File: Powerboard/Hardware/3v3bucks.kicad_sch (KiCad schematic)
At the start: 24 parts, among them IC2 SiC437BED-T1-GE3, Q5 PXP012-30QLJ, Q6 PXP012-30QLJ, U1 LTC4412xS6, U8 LTC4412xS6

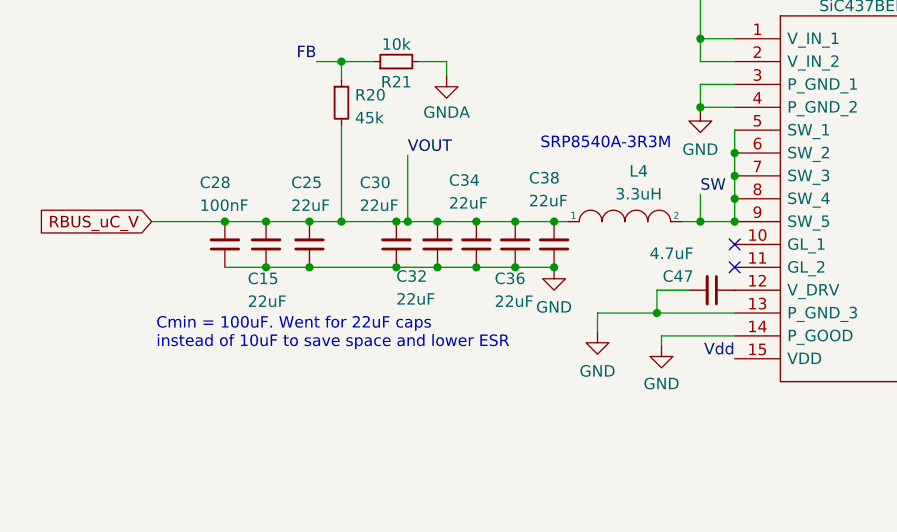
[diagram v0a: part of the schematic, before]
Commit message: removed 100nf cap, pgood pull up
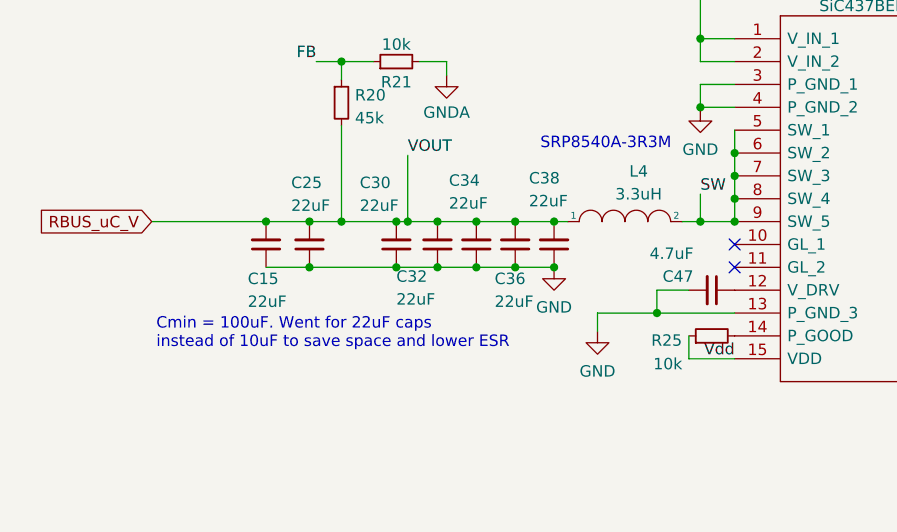
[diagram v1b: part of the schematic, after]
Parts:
- removed C28: 100nF, Capacitor_SMD:C_0402_1005Metric, symbol Device:C_Small
- added R25: 10k, Resistor_SMD:R_0402_1005Metric, symbol Device:R_Small
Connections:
- net GND: no longer IC2.14 (P_GOOD)
- net Vdd: now also R25.1
- new net: IC2.14 (P_GOOD), R25.2
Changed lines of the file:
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@@
   (junction (at 260.858 50.038) (diameter 0) (color 0 0 0 0)
   )
-  (junction (at 63.246 117.348) (diameter 0) (color 0 0 0 0)
-  )
   (junction (at 111.506 112.268) (diameter 0) (color 0 0 0 0)
   )
   (junction (at 63.246 112.268) (diameter 0) (color 0 0 0 0)
-  )
-  (junction (at 58.674 112.268) (diameter 0) (color 0 0 0 0)
   )
   (junction (at 95.25 117.348) (diameter 0) (color 0 0 0 0)
@@
     (stroke (width 0) (type default))
   )
-  (wire (pts (xy 50.546 112.268) (xy 58.674 112.268))
+  (wire (pts (xy 50.546 112.268) (xy 63.246 112.268))
     (stroke (width 0) (type default))
   )
@@
     (stroke (width 0) (type default))
   )
-  (wire (pts (xy 107.188 125.984) (xy 107.188 124.968))
-    (stroke (width 0) (type default))
-  )
   (wire (pts (xy 235.966 77.978) (xy 246.126 77.978))
     (stroke (width 0) (type default))
@@
     (stroke (width 0) (type default))
   )
-  (wire (pts (xy 107.188 124.968) (xy 115.316 124.968))
+  (wire (pts (xy 110.236 127.508) (xy 115.316 127.508))
     (stroke (width 0) (type default))
   )
@@
     (stroke (width 0) (type default))
   )
-  (wire (pts (xy 58.674 112.268) (xy 63.246 112.268))
-    (stroke (width 0) (type default))
-  )
   (wire (pts (xy 86.614 117.348) (xy 90.932 117.348))
     (stroke (width 0) (type default))
   )
-  (wire (pts (xy 58.674 117.348) (xy 63.246 117.348))
-    (stroke (width 0) (type default))
-  )
   (wire (pts (xy 237.236 96.012) (xy 237.236 98.552))
     (stroke (width 0) (type default))
   )
   (wire (pts (xy 276.098 93.472) (xy 262.636 93.472))
+    (stroke (width 0) (type default))
+  )
+  (wire (pts (xy 110.236 124.968) (xy 110.236 127.508))
     (stroke (width 0) (type default))
   )
@@
     )
   )
-  (symbol (lib_id "power:GND") (at 107.188 125.984 0) (unit 1)
-    (in_bom yes) (on_board yes) (dnp no)
-    (property "Reference" "#PWR0105" (at 107.188 132.334 0)
-      (effects (font (size 1.27 1.27)) hide)
-    )
-    (property "Value" "GND" (at 107.188 130.302 0)
-      (effects (font (size 1.27 1.27)))
-    )
-    (property "Footprint" "" (at 107.188 125.984 0)
-      (effects (font (size 1.27 1.27)) hide)
-    )
-    (property "Datasheet" "" (at 107.188 125.984 0)
-      (effects (font (size 1.27 1.27)) hide)
-    )
-    (pin "1")
-    (instances
-      (project "Switcher"
-        (path "/e63e39d7-6ac0-4ffd-8aa3-1841a4541b55/e469982c-3823-4665-9e6d-e90b00c2da09"
-          (reference "#PWR0105") (unit 1)
-        )
-      )
-    )
-  )
   (symbol (lib_id "Power_Management:LTC4412xS6") (at 246.126 67.818 0) (unit 1)
     (in_bom yes) (on_board yes) (dnp no)
@@
     )
   )
-  (symbol (lib_id "Device:C_Small") (at 58.674 114.808 180) (unit 1)
+  (symbol (lib_id "Device:R_Small") (at 112.776 124.968 90) (unit 1)
     (in_bom yes) (on_board yes) (dnp no)
-    (property "Reference" "C28" (at 55.88 107.95 0)
-      (effects (font (size 1.27 1.27)) (justify right))
-    )
-    (property "Value" "100nF" (at 55.88 110.4869 0)
-      (effects (font (size 1.27 1.27)) (justify right))
-    )
-    (property "Footprint" "Capacitor_SMD:C_0402_1005Metric" (at 58.674 114.808 0)
-      (effects (font (size 1.27 1.27)) hide)
-    )
-    (property "Datasheet" "~" (at 58.674 114.808 0)
-      (effects (font (size 1.27 1.27)) hide)
-    )
-    (pin "1")
-    (pin "2")
-    (instances
-      (project "Switcher"
-        (path "/e63e39d7-6ac0-4ffd-8aa3-1841a4541b55/e469982c-3823-4665-9e6d-e90b00c2da09"
-          (reference "C28") (unit 1)
-        )
-      )
+    (property "Reference" "R25" (at 109.474 125.476 90)
+      (effects (font (size 1.27 1.27)) (justify left))
+    )
+    (property "Value" "10k" (at 109.4994 128.0887 90)
+      (effects (font (size 1.27 1.27)) (justify left))
+    )
+    (property "Footprint" "Resistor_SMD:R_0402_1005Metric" (at 112.776 124.968 0)
+      (effects (font (size 1.27 1.27)) hide)
+    )
+    (property "Datasheet" "~" (at 112.776 124.968 0)
+      (effects (font (size 1.27 1.27)) hide)
+    )
+    (pin "1")
+    (pin "2")
+    (instances
+      (project "Switcher"
+        (path "/e63e39d7-6ac0-4ffd-8aa3-1841a4541b55/e469982c-3823-4665-9e6d-e90b00c2da09"
+          (reference "R25") (unit 1)
+        )
+      )

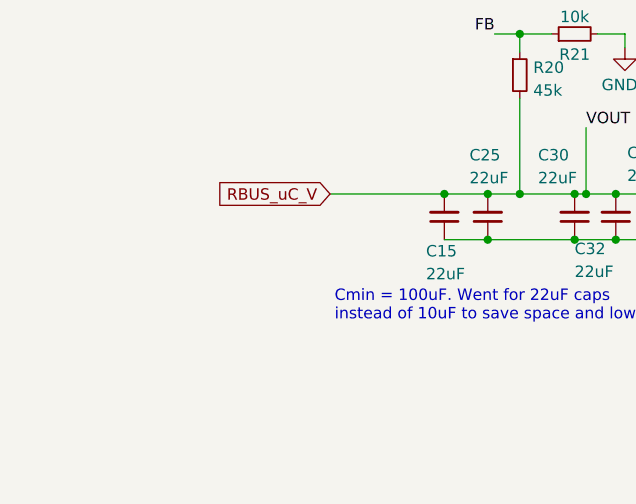
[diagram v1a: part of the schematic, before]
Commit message: 3v3logging moved to buck output
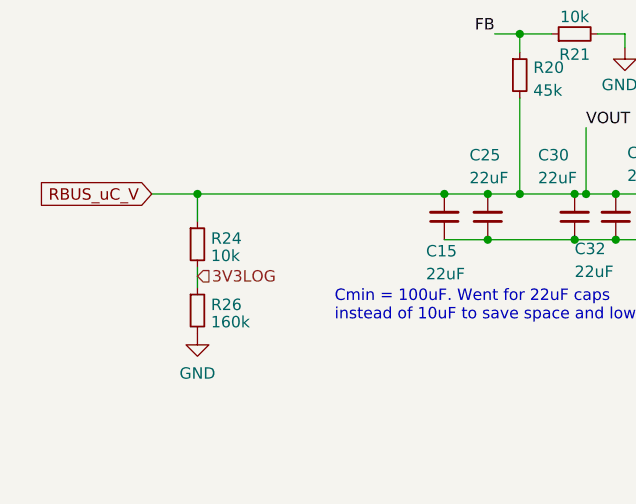
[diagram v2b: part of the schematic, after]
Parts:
- added R24: 10k, Resistor_SMD:R_0402_1005Metric, symbol Device:R_Small
- added R26: 160k, Resistor_SMD:R_0402_1005Metric, symbol Device:R_Small
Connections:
- net GND: now also R26.2
- net RBUS_uC_V: now also R24.1
- new net 3V3LOG: R24.2, R26.1
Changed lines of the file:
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@@
   (junction (at 180.086 107.95) (diameter 0) (color 0 0 0 0)
+  )
+  (junction (at 35.814 112.268) (diameter 0) (color 0 0 0 0)
   )
   (junction (at 260.858 50.038) (diameter 0) (color 0 0 0 0)
@@
     (stroke (width 0) (type default))
   )
-  (wire (pts (xy 50.546 112.268) (xy 63.246 112.268))
+  (wire (pts (xy 30.734 112.268) (xy 35.814 112.268))
     (stroke (width 0) (type default))
   )
@@
     (stroke (width 0) (type default))
   )
+  (wire (pts (xy 35.814 112.268) (xy 63.246 112.268))
+    (stroke (width 0) (type default))
+  )
   (wire (pts (xy 237.236 93.472) (xy 237.236 96.012))
     (stroke (width 0) (type default))
@@
     (stroke (width 0) (type default))
   )
+  (wire (pts (xy 35.814 120.396) (xy 35.814 122.682))
+    (stroke (width 0) (type default))
+  )
   (wire (pts (xy 111.506 83.312) (xy 164.084 83.312))
     (stroke (width 0) (type default))
@@
   )
   (wire (pts (xy 237.744 129.032) (xy 247.904 129.032))
+    (stroke (width 0) (type default))
+  )
+  (wire (pts (xy 35.814 112.268) (xy 35.814 115.316))
     (stroke (width 0) (type default))
   )
@@
     (effects (font (size 1.27 1.27)) (justify right bottom))
   )
-  (global_label "RBUS_uC_V" (shape input) (at 50.546 112.268 180) (fields_autoplaced)
+  (global_label "RBUS_uC_V" (shape input) (at 30.734 112.268 180) (fields_autoplaced)
     (effects (font (size 1.27 1.27)) (justify right))
-    (property "Intersheetrefs" "${INTERSHEET_REFS}" (at 37.6989 112.1886 0)
+    (property "Intersheetrefs" "${INTERSHEET_REFS}" (at 17.8869 112.1886 0)
       (effects (font (size 1.27 1.27)) (justify right) hide)
     )
   )
   (hierarchical_label "USBPOWER" (shape input) (at 258.064 121.412 0) (fields_autoplaced)
+    (effects (font (size 1.27 1.27)) (justify left))
+  )
+  (hierarchical_label "3V3LOG" (shape input) (at 35.814 121.412 0) (fields_autoplaced)
     (effects (font (size 1.27 1.27)) (justify left))
   )
@@
         (path "/e63e39d7-6ac0-4ffd-8aa3-1841a4541b55/e469982c-3823-4665-9e6d-e90b00c2da09"
           (reference "C40") (unit 1)
+        )
+      )
+    )
+  )
+  (symbol (lib_id "power:GND") (at 35.814 127.762 0) (unit 1)
+    (in_bom yes) (on_board yes) (dnp no) (fields_autoplaced)
+    (property "Reference" "#PWR01" (at 35.814 134.112 0)
+      (effects (font (size 1.27 1.27)) hide)
+    )
+    (property "Value" "GND" (at 35.814 132.2054 0)
+      (effects (font (size 1.27 1.27)))
+    )
+    (property "Footprint" "" (at 35.814 127.762 0)
+      (effects (font (size 1.27 1.27)) hide)
+    )
+    (property "Datasheet" "" (at 35.814 127.762 0)
+      (effects (font (size 1.27 1.27)) hide)
+    )
+    (pin "1")
+    (instances
+      (project "Switcher"
+        (path "/e63e39d7-6ac0-4ffd-8aa3-1841a4541b55/133f56f4-a29c-4cbf-87b7-9d99a292e3c0"
+          (reference "#PWR01") (unit 1)
+        )
+        (path "/e63e39d7-6ac0-4ffd-8aa3-1841a4541b55/e469982c-3823-4665-9e6d-e90b00c2da09"
+          (reference "#PWR01") (unit 1)
         )
       )
@@
     )
   )
+  (symbol (lib_id "Device:R_Small") (at 35.814 125.222 0) (unit 1)
+    (in_bom yes) (on_board yes) (dnp no) (fields_autoplaced)
+    (property "Reference" "R26" (at 37.3126 124.5783 0)
+      (effects (font (size 1.27 1.27)) (justify left))
+    )
+    (property "Value" "160k" (at 37.3126 126.4993 0)
+      (effects (font (size 1.27 1.27)) (justify left))
+    )
+    (property "Footprint" "Resistor_SMD:R_0402_1005Metric" (at 35.814 125.222 0)
+      (effects (font (size 1.27 1.27)) hide)
+    )
+    (property "Datasheet" "~" (at 35.814 125.222 0)
+      (effects (font (size 1.27 1.27)) hide)
+    )
+    (pin "1")
+    (pin "2")
+    (instances
+      (project "Switcher"
+        (path "/e63e39d7-6ac0-4ffd-8aa3-1841a4541b55/133f56f4-a29c-4cbf-87b7-9d99a292e3c0"
+          (reference "R26") (unit 1)
+        )
+        (path "/e63e39d7-6ac0-4ffd-8aa3-1841a4541b55/e469982c-3823-4665-9e6d-e90b00c2da09"
+          (reference "R26") (unit 1)
+        )
+      )
+    )
+  )
   (symbol (lib_id "Device:C_Small") (at 68.072 114.808 180) (unit 1)
     (in_bom yes) (on_board yes) (dnp no)
@@
         )
       )
+    )
+  )
+  (symbol (lib_id "Device:R_Small") (at 35.814 117.856 0) (unit 1)
+    (in_bom yes) (on_board yes) (dnp no) (fields_autoplaced)
+    (property "Reference" "R24" (at 37.3126 117.2123 0)
+      (effects (font (size 1.27 1.27)) (justify left))
+    )
+    (property "Value" "10k" (at 37.3126 119.1333 0)
+      (effects (font (size 1.27 1.27)) (justify left))
+    )
+    (property "Footprint" "Resistor_SMD:R_0402_1005Metric" (at 35.814 117.856 0)
+      (effects (font (size 1.27 1.27)) hide)
+    )
+    (property "Datasheet" "~" (at 35.814 117.856 0)
+      (effects (font (size 1.27 1.27)) hide)
+    )
+    (pin "1")
+    (pin "2")
+    (instances
+      (project "Switcher"
+        (path "/e63e39d7-6ac0-4ffd-8aa3-1841a4541b55/133f56f4-a29c-4cbf-87b7-9d99a292e3c0"
+          (reference "R24") (unit 1)
+        )
+        (path "/e63e39d7-6ac0-4ffd-8aa3-1841a4541b55/e469982c-3823-4665-9e6d-e90b00c2da09"
+          (reference "R24") (unit 1)
+        )
+      )

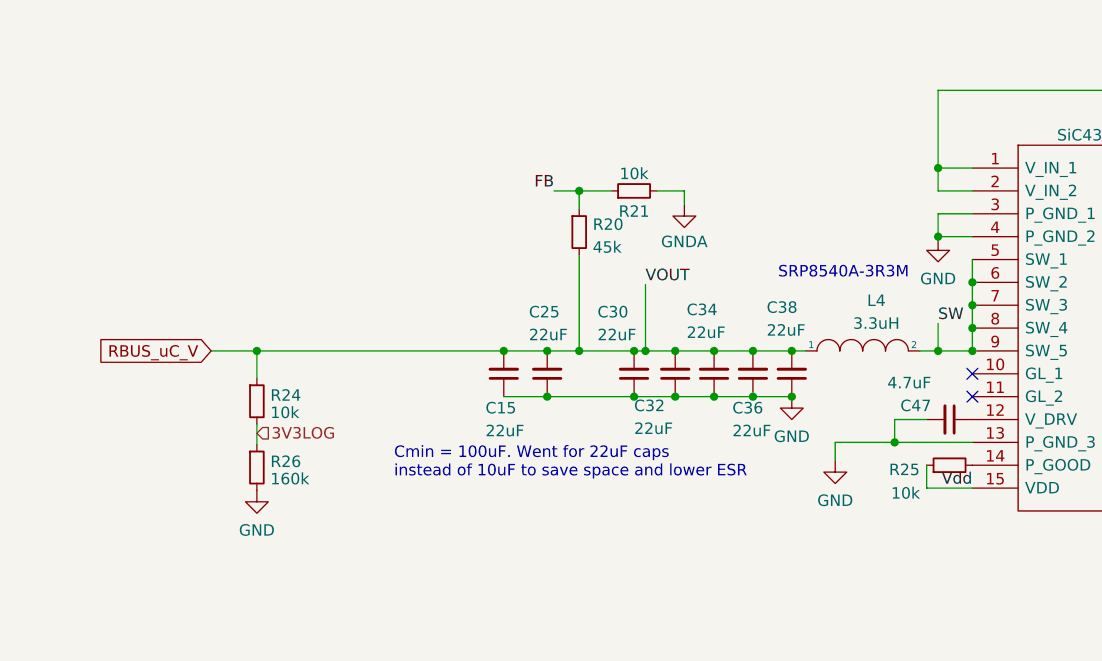
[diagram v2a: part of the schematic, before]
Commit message: new inductor, logging traces rerouted
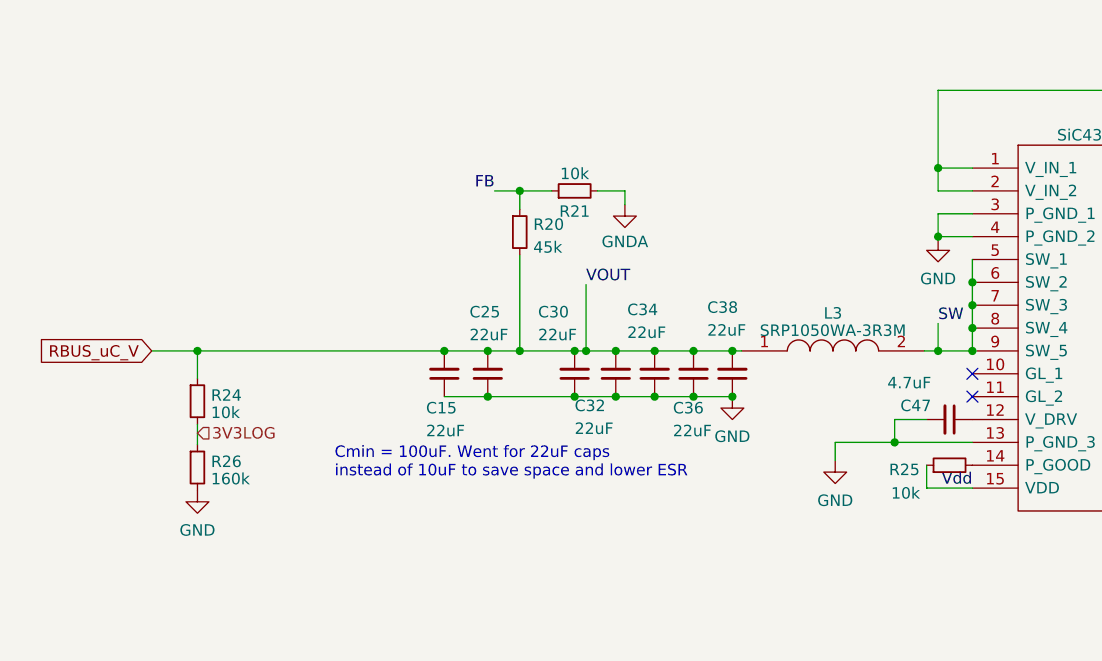
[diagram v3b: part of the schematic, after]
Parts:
- removed L4: 3.3uH, Inductor_SMD:L_10.4x10.4_H4.8, symbol pspice:INDUCTOR
- added L3: SRP1050WA-3R3M, iclr:INDPM110100X540N, symbol iclr:SRP1050WA-3R3M
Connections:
- net RBUS_uC_V: now also L3.1
- net SW: now also L3.2
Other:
- note removed: "SRP8540A-3R3M"
- moved on the sheet: C15, C25, C30, C32, C34, C36, C38, R20, R21, R24, R26

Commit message: added some commands, hardware fixes
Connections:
- net 3V3LOG renamed LogicVoltage
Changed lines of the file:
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@@
     (effects (font (size 1.27 1.27)) (justify left))
   )
-  (hierarchical_label "3V3LOG" (shape input) (at 29.21 121.412 0) (fields_autoplaced)
+  (hierarchical_label "LogicVoltage" (shape input) (at 29.21 121.412 0) (fields_autoplaced)
     (effects (font (size 1.27 1.27)) (justify left))
   )
